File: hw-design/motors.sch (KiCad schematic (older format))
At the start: 24 parts, among them P1 CONN_01X05, P2 CONN_01X05, P4 left_motor, P5 right_motor, P6 CONN_01X05, P7 CONN_01X05, Q1 BC847, U2 TCS3472, U5 drv8835, U6 drv8835, U9 TCS3472

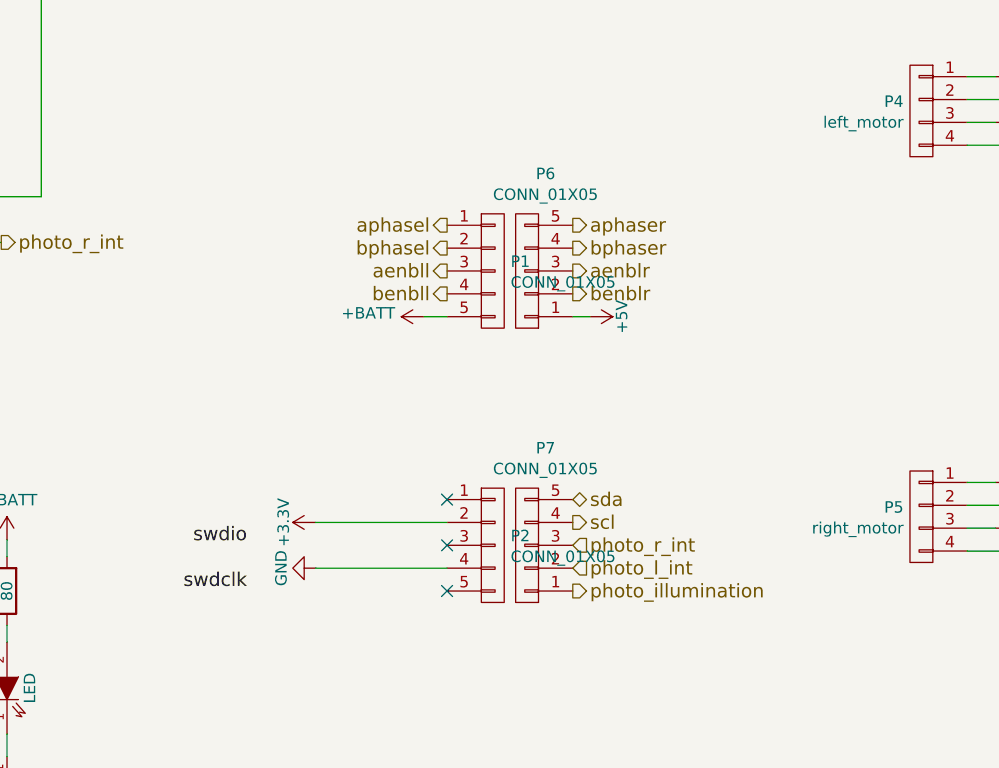
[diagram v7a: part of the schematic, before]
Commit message: Changed to 2 boards layout. On the top one there is only : speaker, IR stuff, RGB led.
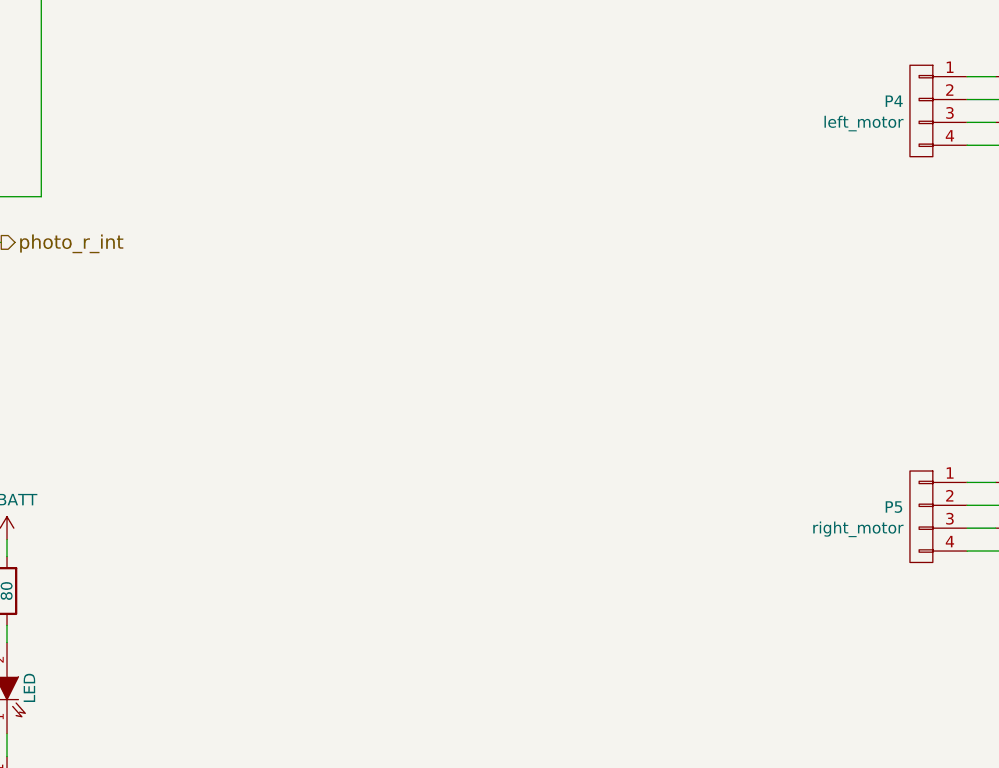
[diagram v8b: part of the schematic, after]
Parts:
- removed P1, P2, P6, P7: CONN_01X05, w_pin_strip:pin_strip_5, symbol CONN_01X05
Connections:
- no-connect marks 5 -> 2
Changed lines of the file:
@@
 	7850 3075 8000 3075
 $Comp
-L GND #PWR29
+L GND #PWR20
 U 1 1 57253FA5
 P 7975 3350
-F 0 "#PWR29" H 7975 3100 50  0001 C CNN
+F 0 "#PWR20" H 7975 3100 50  0001 C CNN
 F 1 "GND" H 7980 3177 50  0000 C CNN
 F 2 "" H 7975 3350 50  0000 C CNN
@@
 	7975 3275 7975 3350
 $Comp
-L +BATT #PWR28
+L +BATT #PWR19
 U 1 1 572546AE
 P 7975 2700
-F 0 "#PWR28" H 7975 2550 50  0001 C CNN
+F 0 "#PWR19" H 7975 2550 50  0001 C CNN
 F 1 "+BATT" H 7990 2873 50  0000 C CNN
 F 2 "" H 7975 2700 50  0000 C CNN
@@
 	7975 2775 7975 2700
 $Comp
-L +3V3 #PWR32
+L +3V3 #PWR23
 U 1 1 572547FA
 P 9425 2450
-F 0 "#PWR32" H 9425 2300 50  0001 C CNN
+F 0 "#PWR23" H 9425 2300 50  0001 C CNN
 F 1 "+3V3" H 9440 2623 50  0000 C CNN
 F 2 "" H 9425 2450 50  0000 C CNN
@@
 $EndComp
 $Comp
-L GND #PWR34
+L GND #PWR25
 U 1 1 57254C5E
 P 10000 2450
-F 0 "#PWR34" H 10000 2200 50  0001 C CNN
+F 0 "#PWR25" H 10000 2200 50  0001 C CNN
 F 1 "GND" H 10005 2277 50  0000 C CNN
 F 2 "" H 10000 2450 50  0000 C CNN
@@
 	7850 4850 8000 4850
 $Comp
-L GND #PWR31
+L GND #PWR22
 U 1 1 572563A3
 P 7975 5125
-F 0 "#PWR31" H 7975 4875 50  0001 C CNN
+F 0 "#PWR22" H 7975 4875 50  0001 C CNN
 F 1 "GND" H 7980 4952 50  0000 C CNN
 F 2 "" H 7975 5125 50  0000 C CNN
@@
 	7975 5050 7975 5125
 $Comp
-L +BATT #PWR30
+L +BATT #PWR21
 U 1 1 572563AB
 P 7975 4475
-F 0 "#PWR30" H 7975 4325 50  0001 C CNN
+F 0 "#PWR21" H 7975 4325 50  0001 C CNN
 F 1 "+BATT" H 7990 4648 50  0000 C CNN
 F 2 "" H 7975 4475 50  0000 C CNN
@@
 	7975 4550 7975 4475
 $Comp
-L +3V3 #PWR33
+L +3V3 #PWR24
 U 1 1 572563B3
 P 9425 4225
-F 0 "#PWR33" H 9425 4075 50  0001 C CNN
+F 0 "#PWR24" H 9425 4075 50  0001 C CNN
 F 1 "+3V3" H 9440 4398 50  0000 C CNN
 F 2 "" H 9425 4225 50  0000 C CNN
@@
 $EndComp
 $Comp
-L GND #PWR35
+L GND #PWR26
 U 1 1 572563C9
 P 10000 4225
-F 0 "#PWR35" H 10000 3975 50  0001 C CNN
+F 0 "#PWR26" H 10000 3975 50  0001 C CNN
 F 1 "GND" H 10005 4052 50  0000 C CNN
 F 2 "" H 10000 4225 50  0000 C CNN
@@
 $EndComp
 $Comp
-L +3.3V #PWR16
+L +3.3V #PWR11
 U 1 1 5810ED32
 P 1475 1925
-F 0 "#PWR16" H 1475 1775 50  0001 C CNN
+F 0 "#PWR11" H 1475 1775 50  0001 C CNN
 F 1 "+3.3V" V 1490 2053 50  0000 L CNN
 F 2 "" H 1475 1925 50  0000 C CNN
@@
 $EndComp
 $Comp
-L GND #PWR18
+L GND #PWR13
 U 1 1 5810ED38
 P 1650 1525
-F 0 "#PWR18" H 1650 1275 50  0001 C CNN
+F 0 "#PWR13" H 1650 1275 50  0001 C CNN
 F 1 "GND" H 1655 1352 50  0000 C CNN
 F 2 "" H 1650 1525 50  0000 C CNN
@@
 $EndComp
 $Comp
-L GND #PWR20
+L GND #PWR15
 U 1 1 5810ED3E
 P 1700 2450
-F 0 "#PWR20" H 1700 2200 50  0001 C CNN
+F 0 "#PWR15" H 1700 2200 50  0001 C CNN
 F 1 "GND" H 1705 2277 50  0000 C CNN
 F 2 "" H 1700 2450 50  0000 C CNN
@@
 $EndComp
 $Comp
-L +3.3V #PWR17
+L +3.3V #PWR12
 U 1 1 5810ED57
 P 1475 3400
-F 0 "#PWR17" H 1475 3250 50  0001 C CNN
+F 0 "#PWR12" H 1475 3250 50  0001 C CNN
 F 1 "+3.3V" V 1490 3528 50  0000 L CNN
 F 2 "" H 1475 3400 50  0000 C CNN
@@
 $EndComp
 $Comp
-L GND #PWR19
+L GND #PWR14
 U 1 1 5810ED5D
 P 1650 3000
-F 0 "#PWR19" H 1650 2750 50  0001 C CNN
+F 0 "#PWR14" H 1650 2750 50  0001 C CNN
 F 1 "GND" H 1655 2827 50  0000 C CNN
 F 2 "" H 1650 3000 50  0000 C CNN
@@
 $EndComp
 $Comp
-L GND #PWR21
+L GND #PWR16
 U 1 1 5810ED63
 P 1700 3925
-F 0 "#PWR21" H 1700 3675 50  0001 C CNN
+F 0 "#PWR16" H 1700 3675 50  0001 C CNN
 F 1 "GND" H 1705 3752 50  0000 C CNN
 F 2 "" H 1700 3925 50  0000 C CNN
@@
 $EndComp
 $Comp
-L GND #PWR23
+L GND #PWR18
 U 1 1 5810ED79
 P 3225 6375
-F 0 "#PWR23" H 3225 6125 50  0001 C CNN
+F 0 "#PWR18" H 3225 6125 50  0001 C CNN
 F 1 "GND" H 3225 6225 50  0000 C CNN
 F 2 "" H 3225 6375 60  0000 C CNN
@@
 	2400 6050 2500 6050
 $Comp
-L +BATT #PWR22
+L +BATT #PWR17
 U 1 1 5810EDAC
 P 3225 4900
-F 0 "#PWR22" H 3225 4750 50  0001 C CNN
+F 0 "#PWR17" H 3225 4750 50  0001 C CNN
 F 1 "+BATT" H 3240 5073 50  0000 C CNN
 F 2 "" H 3225 4900 50  0000 C CNN
@@
 Text Notes 2450 5175 0    60   ~ 0
 10mA @ 80R
-$Comp
-L GND #PWR25
-U 1 1 58138434
-P 4575 5025
-F 0 "#PWR25" H 4575 4775 50  0001 C CNN
-F 1 "GND" H 4575 4875 50  0000 C CNN
-F 2 "" H 4575 5025 60  0000 C CNN
-F 3 "" H 4575 5025 60  0000 C CNN
-	1    4575 5025
-	0    1    1    0
-$EndComp
-$Comp
-L +3.3V #PWR24
-U 1 1 5813843A
-P 4575 4825
-F 0 "#PWR24" H 4575 4675 50  0001 C CNN
-F 1 "+3.3V" H 4575 4965 50  0000 C CNN
-F 2 "" H 4575 4825 60  0000 C CNN
-F 3 "" H 4575 4825 60  0000 C CNN
-	1    4575 4825
-	0    -1   -1   0
-$EndComp
-Wire Wire Line
-	5150 4825 4575 4825
-Wire Wire Line
-	5150 5025 4575 5025
-Text Label 4275 4925 2    60   ~ 0
-swdio
-Text Label 4275 5125 2    60   ~ 0
-swdclk
-Text HLabel 5150 3725 0    60   Output ~ 0
-aenbll
-Text HLabel 5150 3825 0    60   Output ~ 0
-benbll
-Text HLabel 5700 3525 2    60   Output ~ 0
-aphaser
-Text HLabel 5700 3625 2    60   Output ~ 0
-bphaser
-Text HLabel 5700 5025 2    60   Input ~ 0
-photo_l_int
-Text HLabel 5700 4925 2    60   Input ~ 0
-photo_r_int
-Text HLabel 5150 3525 0    60   Output ~ 0
-aphasel
-Text HLabel 5150 3625 0    60   Output ~ 0
-bphasel
-Text HLabel 5700 3825 2    60   Output ~ 0
-benblr
-Text HLabel 5700 3725 2    60   Output ~ 0
-aenblr
-Text HLabel 5700 4825 2    60   Output ~ 0
-scl
-Text HLabel 5700 4725 2    60   BiDi ~ 0
-sda
-Text HLabel 5700 5125 2    60   Output ~ 0
-photo_illumination
-$Comp
-L +BATT #PWR26
-U 1 1 58138462
-P 5050 3925
-F 0 "#PWR26" H 5050 3775 50  0001 C CNN
-F 1 "+BATT" V 5065 4052 50  0000 L CNN
-F 2 "" H 5050 3925 50  0000 C CNN
-F 3 "" H 5050 3925 50  0000 C CNN
-	1    5050 3925
-	0    -1   -1   0
-$EndComp
-$Comp
-L +5V #PWR27
-U 1 1 58138468
-P 5775 3925
-F 0 "#PWR27" H 5775 3775 50  0001 C CNN
-F 1 "+5V" H 5775 4065 50  0000 C CNN
-F 2 "" H 5775 3925 60  0000 C CNN
-F 3 "" H 5775 3925 60  0000 C CNN
-	1    5775 3925
-	0    1    1    0
-$EndComp
-Wire Wire Line
-	5700 3925 5775 3925
-Wire Wire Line
-	5050 3925 5150 3925
-$Comp
-L CONN_01X05 P1
-U 1 1 5813957A
-P 5350 3725
-F 0 "P1" H 5428 3766 50  0000 L CNN
-F 1 "CONN_01X05" H 5428 3675 50  0000 L CNN
-F 2 "w_pin_strip:pin_strip_5" H 5350 3725 50  0001 C CNN
-F 3 "" H 5350 3725 50  0000 C CNN
-	1    5350 3725
-	1    0    0    -1
-$EndComp
-$Comp
-L CONN_01X05 P2
-U 1 1 5813961E
-P 5350 4925
-F 0 "P2" H 5428 4966 50  0000 L CNN
-F 1 "CONN_01X05" H 5428 4875 50  0000 L CNN
-F 2 "w_pin_strip:pin_strip_5" H 5350 4925 50  0001 C CNN
-F 3 "" H 5350 4925 50  0000 C CNN
-	1    5350 4925
-	1    0    0    -1
-$EndComp
-$Comp
-L CONN_01X05 P6
-U 1 1 581396D9
-P 5500 3725
-F 0 "P6" H 5419 3300 50  0000 C CNN
-F 1 "CONN_01X05" H 5419 3391 50  0000 C CNN
-F 2 "w_pin_strip:pin_strip_5" H 5500 3725 50  0001 C CNN
-F 3 "" H 5500 3725 50  0000 C CNN
-	1    5500 3725
-	-1   0    0    1
-$EndComp
-$Comp
-L CONN_01X05 P7
-U 1 1 581397F0
-P 5500 4925
-F 0 "P7" H 5419 4500 50  0000 C CNN
-F 1 "CONN_01X05" H 5419 4591 50  0000 C CNN
-F 2 "w_pin_strip:pin_strip_5" H 5500 4925 50  0001 C CNN
-F 3 "" H 5500 4925 50  0000 C CNN
-	1    5500 4925
-	-1   0    0    1
-$EndComp
-NoConn ~ 5150 4725
-NoConn ~ 5150 4925
-NoConn ~ 5150 5125
 $EndSCHEMATC
